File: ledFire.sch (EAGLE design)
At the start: 29 parts, among them Q1 MUN5235DW1T1G, Q2 MUN5235DW1T1G, U1 MCP1640, U2 ATtiny84A-SSU

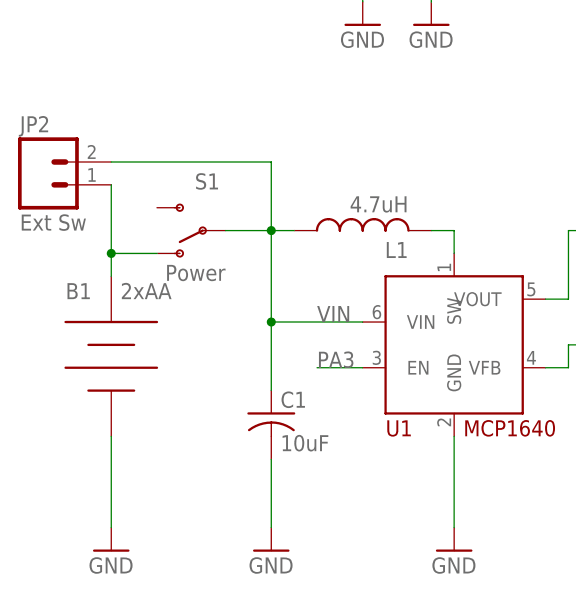
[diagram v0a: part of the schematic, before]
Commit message: v1.1, board corrections.
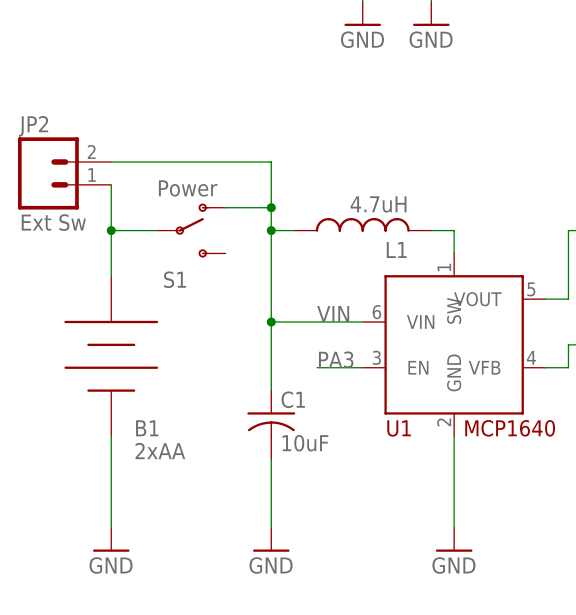
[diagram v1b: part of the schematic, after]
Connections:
- net N$10: now also S1.P; no longer S1.O
- net VIN: now also S1.O; no longer S1.P
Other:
- moved on the sheet: S1
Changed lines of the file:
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@@
 <instance part="U2" gate="G$1" x="86.36" y="104.14"/>
 <instance part="B1" gate="G$1" x="40.64" y="60.96" smashed="yes">
-<attribute name="NAME" x="35.56" y="68.58" size="1.778" layer="95"/>
-<attribute name="VALUE" x="41.656" y="68.58" size="1.778" layer="96"/>
+<attribute name="NAME" x="43.18" y="53.34" size="1.778" layer="95"/>
+<attribute name="VALUE" x="43.18" y="50.8" size="1.778" layer="96"/>
 </instance>
 <instance part="P+4" gate="VCC" x="68.58" y="149.86" smashed="yes">
@@
 <attribute name="VALUE" x="73.66" y="96.52" size="1.778" layer="96"/>
 </instance>
-<instance part="S1" gate="1" x="50.8" y="76.2" rot="R180"/>
+<instance part="S1" gate="1" x="48.26" y="76.2"/>
 <instance part="SJ1" gate="1" x="104.14" y="48.26" rot="R90"/>
 <instance part="SJ2" gate="G$1" x="134.62" y="132.08"/>
@@
 <junction x="58.42" y="66.04"/>
 <junction x="58.42" y="76.2"/>
-<pinref part="S1" gate="1" pin="P"/>
-<wire x1="53.34" y1="76.2" x2="58.42" y2="76.2" width="0.1524" layer="91"/>
 <pinref part="JP2" gate="G$1" pin="2"/>
 <wire x1="40.64" y1="83.82" x2="58.42" y2="83.82" width="0.1524" layer="91"/>
-<wire x1="58.42" y1="83.82" x2="58.42" y2="76.2" width="0.1524" layer="91"/>
+<wire x1="58.42" y1="83.82" x2="58.42" y2="78.74" width="0.1524" layer="91"/>
+<pinref part="S1" gate="1" pin="O"/>
+<wire x1="58.42" y1="78.74" x2="58.42" y2="76.2" width="0.1524" layer="91"/>
+<wire x1="53.34" y1="78.74" x2="58.42" y2="78.74" width="0.1524" layer="91"/>
+<junction x="58.42" y="78.74"/>
 </segment>
 </net>
@@
 <segment>
 <pinref part="B1" gate="G$1" pin="POS"/>
-<wire x1="40.64" y1="73.66" x2="40.64" y2="71.12" width="0.1524" layer="91"/>
-<pinref part="S1" gate="1" pin="O"/>
-<wire x1="40.64" y1="73.66" x2="45.72" y2="73.66" width="0.1524" layer="91"/>
 <pinref part="JP2" gate="G$1" pin="1"/>
-<wire x1="40.64" y1="81.28" x2="40.64" y2="73.66" width="0.1524" layer="91"/>
-<junction x="40.64" y="73.66"/>
-</segment>
-</net>
+<wire x1="40.64" y1="81.28" x2="40.64" y2="76.2" width="0.1524" layer="91"/>
+<pinref part="S1" gate="1" pin="P"/>
+<wire x1="40.64" y1="76.2" x2="40.64" y2="71.12" width="0.1524" layer="91"/>
+<wire x1="45.72" y1="76.2" x2="40.64" y2="76.2" width="0.1524" layer="91"/>
+<junction x="40.64" y="76.2"/>
+</segment>
+</net>

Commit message: Update board and schematic images.
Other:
- note added: "CC BY-SA"
- note added: "LED PWM Fire Effect"
- note added: "LED PWM Fire Effect by Jack Christensen is licensed under CC BY-SA 4.0 http://creativecommons.org/licenses/by-sa/4.0/"
- note added: "by Jack Christensen"
- moved on the sheet: B1, C1, C2, C3, C4, D1, D2, D3, D4, JP1, JP2, L1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

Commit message: Update part list.
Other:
- note added: "v1.1"
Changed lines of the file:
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@@
 under CC BY-SA 4.0 http://creativecommons.org/licenses/by-sa/4.0/                       </text>
 <text x="15.24" y="20.32" size="3.81" layer="94" ratio="12">CC BY-SA</text>
+<text x="261.62" y="7.62" size="2.54" layer="94" ratio="12">v1.1</text>
 </plain>
 <instances>

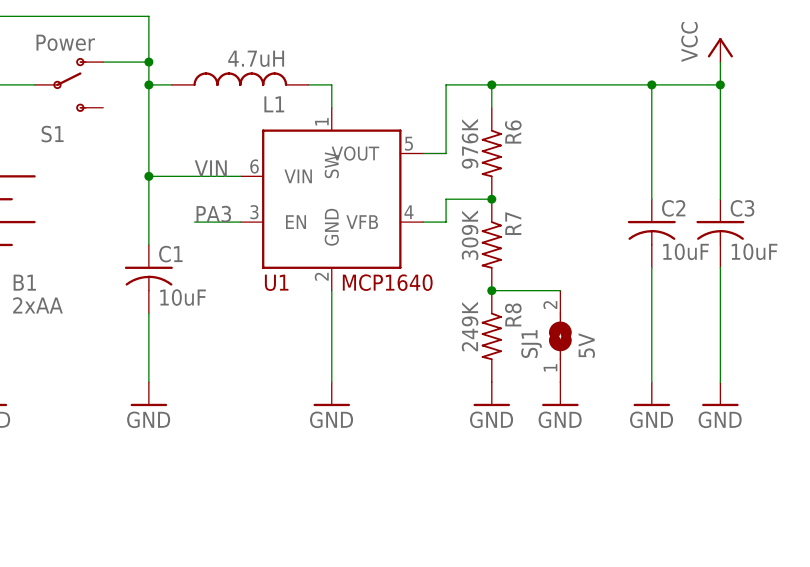
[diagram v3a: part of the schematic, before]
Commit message: Tweak SOT363 footprint.
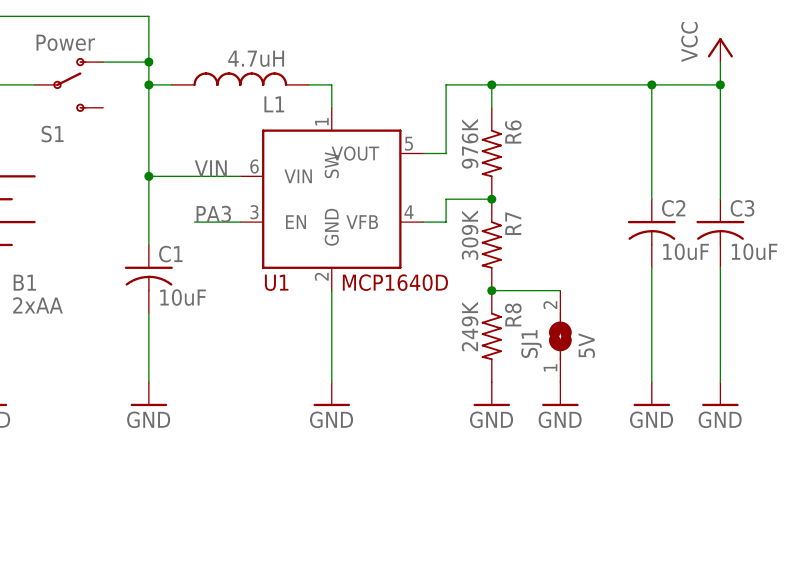
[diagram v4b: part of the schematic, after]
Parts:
- U1: value MCP1640 -> MCP1640D
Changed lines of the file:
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@@
 <parts>
 <part name="FRAME1" library="frames" deviceset="FRAME_A_L" device="" value="frame"/>
-<part name="U1" library="_jc" deviceset="MCP1640" device="" value="MCP1640"/>
+<part name="U1" library="_jc" deviceset="MCP1640" device="" value="MCP1640D"/>
 <part name="R6" library="_jc" deviceset="R-US_" device="M0805" value="976K"/>
 <part name="R7" library="_jc" deviceset="R-US_" device="M0805" value="309K"/>
